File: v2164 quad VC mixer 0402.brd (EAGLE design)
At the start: 30.5 x 13.7 mm, 33 parts, among them IC1 TL072JD

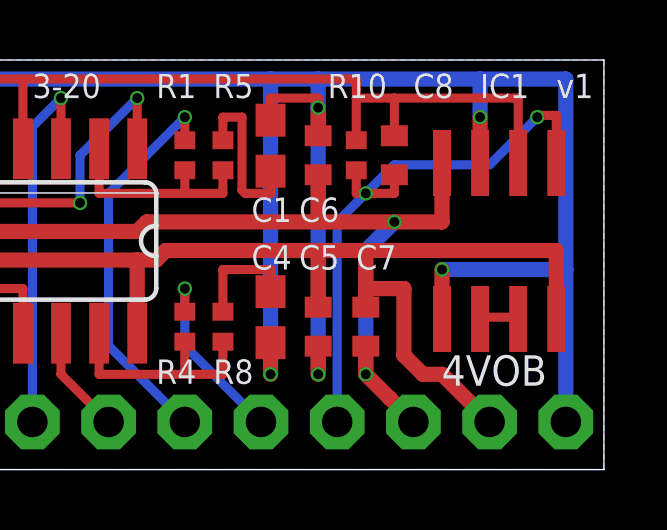
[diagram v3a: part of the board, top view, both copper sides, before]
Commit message: Added optional shottky diodes
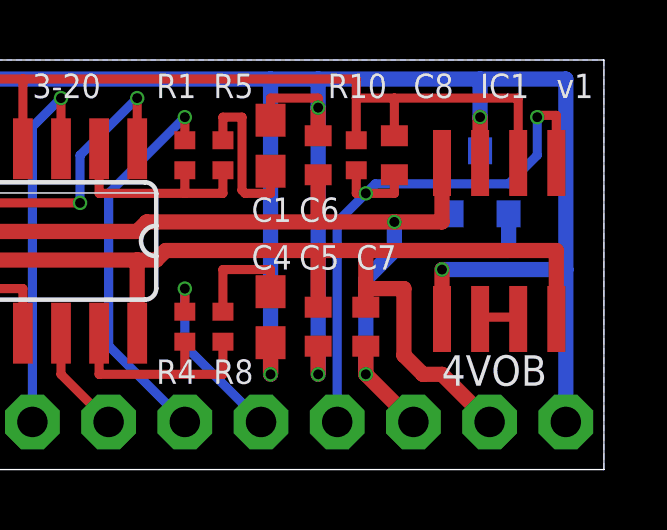
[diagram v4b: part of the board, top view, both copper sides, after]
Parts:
- added Q1: BA854SW, joakim:SOT23-3J
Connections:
- net -15V: now also Q1.1
- net GND: now also Q1.3
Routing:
- net -15V: track 33.8 -> 38.9 mm
- net GND: track 86.6 -> 87.7 mm
- net OUT: track 19.7 -> 20.4 mm
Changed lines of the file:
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@@
 <layer number="2" name="Route2" color="16" fill="1" visible="no" active="no"/>
 <layer number="15" name="Route15" color="23" fill="1" visible="no" active="no"/>
-<layer number="16" name="Bottom" color="1" fill="1" visible="no" active="yes"/>
+<layer number="16" name="Bottom" color="1" fill="1" visible="yes" active="yes"/>
 <layer number="17" name="Pads" color="2" fill="1" visible="yes" active="yes"/>
 <layer number="18" name="Vias" color="2" fill="1" visible="yes" active="yes"/>
 <layer number="19" name="Unrouted" color="6" fill="1" visible="yes" active="yes"/>
 <layer number="20" name="Dimension" color="24" fill="1" visible="yes" active="yes"/>
-<layer number="21" name="tPlace" color="7" fill="1" visible="yes" active="yes"/>
-<layer number="22" name="bPlace" color="7" fill="1" visible="no" active="yes"/>
-<layer number="23" name="tOrigins" color="15" fill="1" visible="yes" active="yes"/>
-<layer number="24" name="bOrigins" color="15" fill="1" visible="no" active="yes"/>
-<layer number="25" name="tNames" color="7" fill="1" visible="yes" active="yes"/>
-<layer number="26" name="bNames" color="7" fill="1" visible="no" active="yes"/>
+<layer number="21" name="tPlace" color="7" fill="1" visible="no" active="yes"/>
+<layer number="22" name="bPlace" color="7" fill="1" visible="yes" active="yes"/>
+<layer number="23" name="tOrigins" color="15" fill="1" visible="no" active="yes"/>
+<layer number="24" name="bOrigins" color="15" fill="1" visible="yes" active="yes"/>
+<layer number="25" name="tNames" color="7" fill="1" visible="no" active="yes"/>
+<layer number="26" name="bNames" color="7" fill="1" visible="yes" active="yes"/>
 <layer number="27" name="tValues" color="7" fill="1" visible="no" active="yes"/>
 <layer number="28" name="bValues" color="7" fill="1" visible="no" active="yes"/>
@@
 <layer number="37" name="tTest" color="7" fill="1" visible="no" active="yes"/>
 <layer number="38" name="bTest" color="7" fill="1" visible="no" active="yes"/>
-<layer number="39" name="tKeepout" color="4" fill="11" visible="yes" active="yes"/>
-<layer number="40" name="bKeepout" color="1" fill="11" visible="no" active="yes"/>
-<layer number="41" name="tRestrict" color="4" fill="10" visible="yes" active="yes"/>
-<layer number="42" name="bRestrict" color="1" fill="10" visible="no" active="yes"/>
+<layer number="39" name="tKeepout" color="4" fill="11" visible="no" active="yes"/>
+<layer number="40" name="bKeepout" color="1" fill="11" visible="yes" active="yes"/>
+<layer number="41" name="tRestrict" color="4" fill="10" visible="no" active="yes"/>
+<layer number="42" name="bRestrict" color="1" fill="10" visible="yes" active="yes"/>
 <layer number="43" name="vRestrict" color="2" fill="10" visible="no" active="yes"/>
 <layer number="44" name="Drills" color="7" fill="1" visible="no" active="yes"/>
@@
 <layer number="49" name="Reference" color="7" fill="1" visible="no" active="yes"/>
 <layer number="50" name="dxf" color="7" fill="1" visible="no" active="no"/>
-<layer number="51" name="tDocu" color="7" fill="1" visible="yes" active="yes"/>
-<layer number="52" name="bDocu" color="7" fill="1" visible="no" active="yes"/>
+<layer number="51" name="tDocu" color="7" fill="1" visible="no" active="yes"/>
+<layer number="52" name="bDocu" color="7" fill="1" visible="yes" active="yes"/>
 <layer number="53" name="tGND_GNDA" color="7" fill="9" visible="no" active="no"/>
 <layer number="54" name="bGND_GNDA" color="1" fill="9" visible="no" active="no"/>
@@
 </element>
 <element name="U$1" library="joakim" package="XONIK_LOGO_20" value="" x="21.59" y="7.9375" smashed="yes" rot="MR0"/>
+<element name="Q1" library="joakim" package="SOT23-3J" value="BA854SW" x="26.3525" y="9.525" smashed="yes" rot="MR0">
+<attribute name="NAME" x="27.178" y="11.303" size="0.4064" layer="26" rot="MR0"/>
+<attribute name="VALUE" x="27.3685" y="9.3345" size="0.4064" layer="28" rot="MR0"/>
+</element>
 </elements>
 <signals>
@@
 <via x="25.0825" y="6.6675" extent="1-16" drill="0.3302"/>
 <wire x1="25.0825" y1="6.6675" x2="29.21" y2="6.6675" width="0.508" layer="16"/>
+<contactref element="Q1" pad="3"/>
+<wire x1="26.3525" y1="10.625" x2="26.3525" y2="11.7475" width="0.508" layer="16"/>
 </signal>
 <signal name="N$5">
@@
 <wire x1="28.8925" y1="11.8075" x2="28.3175" y2="11.8075" width="0.3048" layer="1"/>
 <via x="28.2575" y="11.7475" extent="1-16" drill="0.3302"/>
-<wire x1="28.2575" y1="11.7475" x2="26.67" y2="10.16" width="0.3048" layer="16"/>
-<wire x1="26.67" y1="10.16" x2="23.495" y2="10.16" width="0.3048" layer="16"/>
-<wire x1="23.495" y1="10.16" x2="22.5425" y2="9.2075" width="0.3048" layer="16"/>
+<wire x1="28.2575" y1="11.7475" x2="28.2575" y2="10.4775" width="0.3048" layer="16"/>
+<wire x1="28.2575" y1="10.4775" x2="27.305" y2="9.525" width="0.3048" layer="16"/>
+<wire x1="27.305" y1="9.525" x2="22.86" y2="9.525" width="0.3048" layer="16"/>
+<wire x1="22.86" y1="9.525" x2="22.5425" y2="9.2075" width="0.3048" layer="16"/>
 <via x="22.5425" y="9.2075" extent="1-16" drill="0.3302"/>
 <wire x1="22.5425" y1="9.2075" x2="23.495" y2="9.2075" width="0.3048" layer="1"/>
@@
 <wire x1="22.5425" y1="4.1125" x2="22.5425" y2="3.175" width="0.508" layer="1"/>
 <via x="22.5425" y="3.175" extent="1-16" drill="0.3302"/>
-<wire x1="23.495" y1="8.255" x2="22.5425" y2="7.3025" width="0.508" layer="16"/>
-<wire x1="22.5425" y1="7.3025" x2="22.5425" y2="3.175" width="0.508" layer="16"/>
+<wire x1="23.495" y1="7.3025" x2="22.5425" y2="6.35" width="0.508" layer="16"/>
+<wire x1="22.5425" y1="6.35" x2="22.5425" y2="3.175" width="0.508" layer="16"/>
 <via x="23.495" y="8.255" extent="1-16" drill="0.3302"/>
 <wire x1="15.24" y1="8.255" x2="14.9225" y2="7.9375" width="0.508" layer="1"/>
@@
 <wire x1="6.0325" y1="6.0325" x2="6.0325" y2="4.5466" width="0.508" layer="1"/>
 <wire x1="14.9225" y1="7.9375" x2="7.62" y2="7.9375" width="0.508" layer="1"/>
-<wire x1="24.13" y1="1.5875" x2="23.33625" y2="2.38125" width="0.508" layer="1"/>
-<wire x1="23.33625" y1="2.38125" x2="22.5425" y2="3.175" width="0.508" layer="1"/>
+<wire x1="24.13" y1="1.5875" x2="22.5425" y2="3.175" width="0.508" layer="1"/>
+<contactref element="Q1" pad="1"/>
+<wire x1="27.3025" y1="8.525" x2="27.305" y2="8.5225" width="0.508" layer="16"/>
+<wire x1="27.305" y1="8.5225" x2="27.305" y2="7.3025" width="0.508" layer="16"/>
+<wire x1="27.305" y1="7.3025" x2="23.495" y2="7.3025" width="0.508" layer="16"/>
+<wire x1="23.495" y1="7.3025" x2="23.495" y2="8.255" width="0.508" layer="16"/>
 </signal>
 <signal name="N$1">

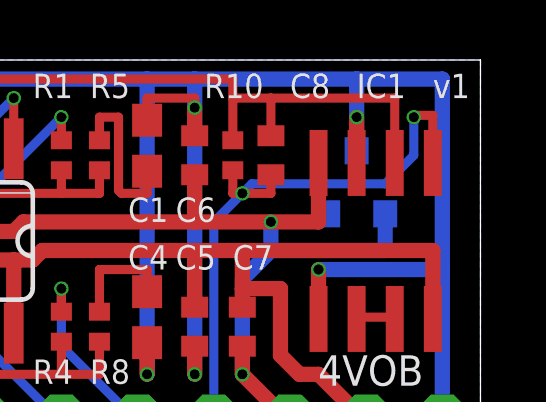
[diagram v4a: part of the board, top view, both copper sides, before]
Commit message: Fixed some silk screen errors and replaced pads with some that solder slightly better
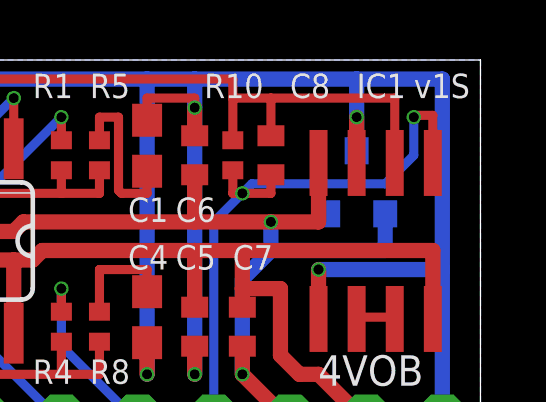
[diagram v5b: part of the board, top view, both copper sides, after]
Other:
- board text added: "v1S"
- board text removed: "v1"
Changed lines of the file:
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@@
 <layer number="19" name="Unrouted" color="6" fill="1" visible="yes" active="yes"/>
 <layer number="20" name="Dimension" color="24" fill="1" visible="yes" active="yes"/>
-<layer number="21" name="tPlace" color="7" fill="1" visible="no" active="yes"/>
+<layer number="21" name="tPlace" color="7" fill="1" visible="yes" active="yes"/>
 <layer number="22" name="bPlace" color="7" fill="1" visible="yes" active="yes"/>
-<layer number="23" name="tOrigins" color="15" fill="1" visible="no" active="yes"/>
+<layer number="23" name="tOrigins" color="15" fill="1" visible="yes" active="yes"/>
 <layer number="24" name="bOrigins" color="15" fill="1" visible="yes" active="yes"/>
-<layer number="25" name="tNames" color="7" fill="1" visible="no" active="yes"/>
-<layer number="26" name="bNames" color="7" fill="1" visible="yes" active="yes"/>
+<layer number="25" name="tNames" color="7" fill="1" visible="yes" active="yes"/>
+<layer number="26" name="bNames" color="7" fill="1" visible="no" active="yes"/>
 <layer number="27" name="tValues" color="7" fill="1" visible="no" active="yes"/>
 <layer number="28" name="bValues" color="7" fill="1" visible="no" active="yes"/>
@@
 <layer number="37" name="tTest" color="7" fill="1" visible="no" active="yes"/>
 <layer number="38" name="bTest" color="7" fill="1" visible="no" active="yes"/>
-<layer number="39" name="tKeepout" color="4" fill="11" visible="no" active="yes"/>
+<layer number="39" name="tKeepout" color="4" fill="11" visible="yes" active="yes"/>
 <layer number="40" name="bKeepout" color="1" fill="11" visible="yes" active="yes"/>
-<layer number="41" name="tRestrict" color="4" fill="10" visible="no" active="yes"/>
+<layer number="41" name="tRestrict" color="4" fill="10" visible="yes" active="yes"/>
 <layer number="42" name="bRestrict" color="1" fill="10" visible="yes" active="yes"/>
 <layer number="43" name="vRestrict" color="2" fill="10" visible="no" active="yes"/>
@@
 <layer number="49" name="Reference" color="7" fill="1" visible="no" active="yes"/>
 <layer number="50" name="dxf" color="7" fill="1" visible="no" active="no"/>
-<layer number="51" name="tDocu" color="7" fill="1" visible="no" active="yes"/>
+<layer number="51" name="tDocu" color="7" fill="1" visible="yes" active="yes"/>
 <layer number="52" name="bDocu" color="7" fill="1" visible="yes" active="yes"/>
 <layer number="53" name="tGND_GNDA" color="7" fill="9" visible="no" active="no"/>
@@
 <text x="28.575" y="3.81" size="1.016" layer="25" font="vector" rot="R180">4VOB</text>
 <text x="11.43" y="12.3825" size="0.8128" layer="25" font="vector">3-20</text>
-<text x="28.8925" y="12.3825" size="0.8128" layer="25" font="vector">v1</text>
+<text x="28.2575" y="12.3825" size="0.8128" layer="25" font="vector">v1S</text>
 <text x="0.635" y="3.4925" size="1.27" layer="26" font="vector" rot="MR90">I1</text>
 <text x="3.175" y="3.4925" size="1.27" layer="26" font="vector" rot="MR90">I2</text>
